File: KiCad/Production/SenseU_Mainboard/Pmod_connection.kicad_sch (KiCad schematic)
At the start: 1 part, among them J4 90122-0126

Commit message: assigning components
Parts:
- renumbered J4 to J3
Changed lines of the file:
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@@
         )
         (path "/43872b54-cf9c-4c7b-870d-631baccef0c0/915563dd-e56c-42ce-a954-58d654408565/fb835e06-d907-4f71-88e6-a872b0f9d18c"
-          (reference "#PWR064") (unit 1)
+          (reference "#PWR036") (unit 1)
         )
       )
@@
   (symbol (lib_id "SensU_Microphone_parts:90122-0126") (at 130.302 59.944 0) (unit 1)
     (in_bom yes) (on_board yes) (dnp no) (fields_autoplaced)
-    (property "Reference" "J4" (at 141.732 53.594 0)
+    (property "Reference" "J3" (at 141.732 53.594 0)
       (effects (font (size 1.27 1.27)))
     )
@@
       (project "SenseU_Mainboard"
         (path "/43872b54-cf9c-4c7b-870d-631baccef0c0/915563dd-e56c-42ce-a954-58d654408565/fb835e06-d907-4f71-88e6-a872b0f9d18c"
-          (reference "J4") (unit 1)
+          (reference "J3") (unit 1)
         )
       )
@@
         )
         (path "/43872b54-cf9c-4c7b-870d-631baccef0c0/915563dd-e56c-42ce-a954-58d654408565/fb835e06-d907-4f71-88e6-a872b0f9d18c"
-          (reference "#PWR065") (unit 1)
+          (reference "#PWR037") (unit 1)
         )
       )

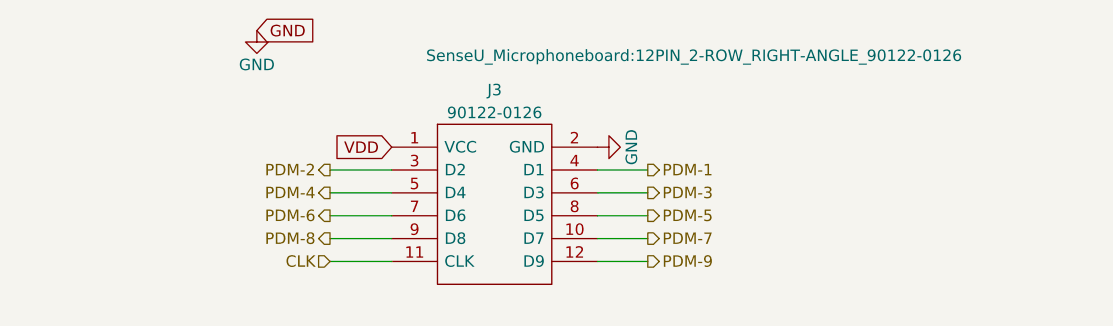
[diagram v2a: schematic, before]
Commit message: routing SenseU done
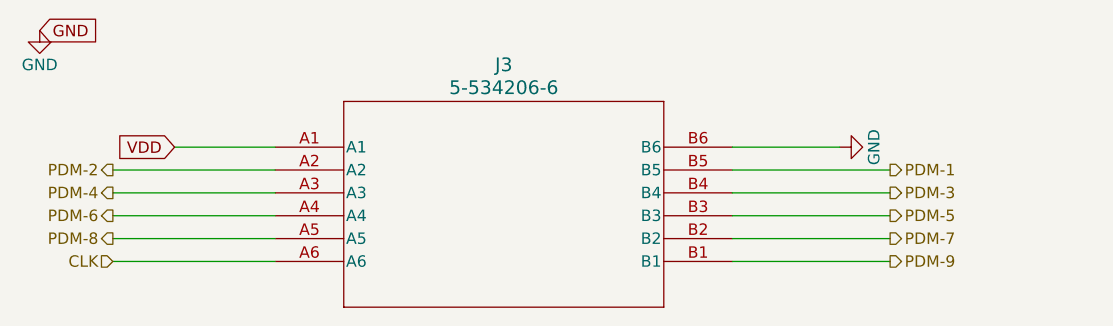
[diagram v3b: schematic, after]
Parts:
- removed J3: 90122-0126, SenseU_Microphoneboard:12PIN_2-ROW_RIGHT-ANGLE_90122-0126, symbol SensU_Microphone_parts:90122-0126
- added J3: 5-534206-6, PMOD:5-534206-6_TYC, symbol 2023-06-17_18-13-39:5-534206-6
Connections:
- net CLK: now also J3.A6
- net GND: now also J3.B6
- net PDM-1: now also J3.B5
- net PDM-2: now also J3.A2
- net PDM-3: now also J3.B4
- net PDM-4: now also J3.A3
- net PDM-5: now also J3.B3
- net PDM-6: now also J3.A4
- net PDM-7: now also J3.B2
- net PDM-8: now also J3.A5
- net PDM-9: now also J3.B1
- net VDD: now also J3.A1
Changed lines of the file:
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@@
 (kicad_sch (version 20230121) (generator eeschema)
   (paper "A4")
-  (wire (pts (xy 123.444 72.644) (xy 130.302 72.644))
+  (wire (pts (xy 99.314 72.644) (xy 117.348 72.644))
     (stroke (width 0) (type default))
   )
-  (wire (pts (xy 123.444 65.024) (xy 130.302 65.024))
+  (wire (pts (xy 99.314 65.024) (xy 117.348 65.024))
     (stroke (width 0) (type default))
   )
-  (wire (pts (xy 153.162 65.024) (xy 158.75 65.024))
+  (wire (pts (xy 106.172 59.944) (xy 117.348 59.944))
     (stroke (width 0) (type default))
   )
-  (wire (pts (xy 123.444 67.564) (xy 130.302 67.564))
+  (wire (pts (xy 168.148 65.024) (xy 185.674 65.024))
     (stroke (width 0) (type default))
   )
-  (wire (pts (xy 153.162 70.104) (xy 158.75 70.104))
+  (wire (pts (xy 99.314 67.564) (xy 117.348 67.564))
     (stroke (width 0) (type default))
   )
-  (wire (pts (xy 153.162 62.484) (xy 158.75 62.484))
+  (wire (pts (xy 168.148 70.104) (xy 185.674 70.104))
     (stroke (width 0) (type default))
   )
-  (wire (pts (xy 153.162 72.644) (xy 158.75 72.644))
+  (wire (pts (xy 168.148 62.484) (xy 185.674 62.484))
     (stroke (width 0) (type default))
   )
-  (wire (pts (xy 123.444 62.484) (xy 130.302 62.484))
+  (wire (pts (xy 99.314 62.484) (xy 117.348 62.484))
     (stroke (width 0) (type default))
   )
-  (wire (pts (xy 153.162 67.564) (xy 158.75 67.564))
+  (wire (pts (xy 168.148 67.564) (xy 185.674 67.564))
     (stroke (width 0) (type default))
   )
-  (wire (pts (xy 123.444 70.104) (xy 130.302 70.104))
+  (wire (pts (xy 168.148 72.644) (xy 185.674 72.644))
     (stroke (width 0) (type default))
   )
-  (global_label "VDD" (shape input) (at 130.302 59.944 180) (fields_autoplaced)
+  (wire (pts (xy 180.086 59.944) (xy 168.148 59.944))
+    (stroke (width 0) (type default))
+  )
+  (wire (pts (xy 99.314 70.104) (xy 117.348 70.104))
+    (stroke (width 0) (type default))
+  )
+  (global_label "VDD" (shape input) (at 106.172 59.944 180) (fields_autoplaced)
     (effects (font (size 1.27 1.27)) (justify right))
-    (property "Intersheetrefs" "${INTERSHEET_REFS}" (at 123.9435 59.944 0)
+    (property "Intersheetrefs" "${INTERSHEET_REFS}" (at 99.8135 59.944 0)
       (effects (font (size 1.27 1.27)) (justify right) hide)
     )
   )
-  (global_label "GND" (shape input) (at 115.316 46.99 0) (fields_autoplaced)
+  (global_label "GND" (shape input) (at 91.186 46.99 0) (fields_autoplaced)
     (effects (font (size 1.27 1.27)) (justify left))
-    (property "Intersheetrefs" "${INTERSHEET_REFS}" (at 121.8742 46.99 0)
+    (property "Intersheetrefs" "${INTERSHEET_REFS}" (at 97.7442 46.99 0)
       (effects (font (size 1.27 1.27)) (justify left) hide)
     )
   )
-  (hierarchical_label "PDM-7" (shape output) (at 158.75 70.104 0) (fields_autoplaced)
+  (hierarchical_label "PDM-7" (shape output) (at 185.674 70.104 0) (fields_autoplaced)
     (effects (font (size 1.27 1.27)) (justify left))
   )
-  (hierarchical_label "PDM-3" (shape output) (at 158.75 65.024 0) (fields_autoplaced)
+  (hierarchical_label "PDM-3" (shape output) (at 185.674 65.024 0) (fields_autoplaced)
     (effects (font (size 1.27 1.27)) (justify left))
   )
-  (hierarchical_label "PDM-8" (shape output) (at 123.444 70.104 180) (fields_autoplaced)
+  (hierarchical_label "PDM-8" (shape output) (at 99.314 70.104 180) (fields_autoplaced)
     (effects (font (size 1.27 1.27)) (justify right))
   )
-  (hierarchical_label "PDM-2" (shape output) (at 123.444 62.484 180) (fields_autoplaced)
+  (hierarchical_label "PDM-2" (shape output) (at 99.314 62.484 180) (fields_autoplaced)
     (effects (font (size 1.27 1.27)) (justify right))
   )
-  (hierarchical_label "PDM-5" (shape output) (at 158.75 67.564 0) (fields_autoplaced)
+  (hierarchical_label "PDM-5" (shape output) (at 185.674 67.564 0) (fields_autoplaced)
     (effects (font (size 1.27 1.27)) (justify left))
   )
-  (hierarchical_label "PDM-4" (shape output) (at 123.444 65.024 180) (fields_autoplaced)
+  (hierarchical_label "PDM-4" (shape output) (at 99.314 65.024 180) (fields_autoplaced)
     (effects (font (size 1.27 1.27)) (justify right))
   )
-  (hierarchical_label "CLK" (shape input) (at 123.444 72.644 180) (fields_autoplaced)
+  (hierarchical_label "CLK" (shape input) (at 99.314 72.644 180) (fields_autoplaced)
     (effects (font (size 1.27 1.27)) (justify right))
   )
-  (hierarchical_label "PDM-6" (shape output) (at 123.444 67.564 180) (fields_autoplaced)
+  (hierarchical_label "PDM-6" (shape output) (at 99.314 67.564 180) (fields_autoplaced)
     (effects (font (size 1.27 1.27)) (justify right))
   )
-  (hierarchical_label "PDM-9" (shape output) (at 158.75 72.644 0) (fields_autoplaced)
+  (hierarchical_label "PDM-9" (shape output) (at 185.674 72.644 0) (fields_autoplaced)
     (effects (font (size 1.27 1.27)) (justify left))
   )
-  (hierarchical_label "PDM-1" (shape output) (at 158.75 62.484 0) (fields_autoplaced)
+  (hierarchical_label "PDM-1" (shape output) (at 185.674 62.484 0) (fields_autoplaced)
     (effects (font (size 1.27 1.27)) (justify left))
   )
-  (symbol (lib_id "power:GND") (at 115.316 46.99 0) (unit 1)
+  (symbol (lib_id "power:GND") (at 91.186 46.99 0) (unit 1)
     (in_bom yes) (on_board yes) (dnp no)
-    (property "Reference" "#PWR024" (at 115.316 53.34 0)
+    (property "Reference" "#PWR024" (at 91.186 53.34 0)
       (effects (font (size 1.27 1.27)) hide)
     )
-    (property "Value" "GND" (at 115.316 50.8 0)
+    (property "Value" "GND" (at 91.186 50.8 0)
       (effects (font (size 1.27 1.27)))
     )
-    (property "Footprint" "" (at 115.316 46.99 0)
+    (property "Footprint" "" (at 91.186 46.99 0)
       (effects (font (size 1.27 1.27)) hide)
     )
-    (property "Datasheet" "" (at 115.316 46.99 0)
+    (property "Datasheet" "" (at 91.186 46.99 0)
       (effects (font (size 1.27 1.27)) hide)
     )
@@
     )
   )
-  (symbol (lib_id "SensU_Microphone_parts:90122-0126") (at 130.302 59.944 0) (unit 1)
+  (symbol (lib_id "2023-06-17_18-13-39:5-534206-6") (at 117.348 59.944 0) (unit 1)
     (in_bom yes) (on_board yes) (dnp no) (fields_autoplaced)
-    (property "Reference" "J3" (at 141.732 53.594 0)
-      (effects (font (size 1.27 1.27)))
+    (property "Reference" "J3" (at 142.748 50.8 0)
+      (effects (font (size 1.524 1.524)))
     )
-    (property "Value" "90122-0126" (at 141.732 56.134 0)
-      (effects (font (size 1.27 1.27)))
+    (property "Value" "5-534206-6" (at 142.748 53.34 0)
+      (effects (font (size 1.524 1.524)))
     )
-    (property "Footprint" "SenseU_Microphoneboard:12PIN_2-ROW_RIGHT-ANGLE_90122-0126" (at 134.112 49.784 0)
-      (effects (font (size 1.27 1.27)) (justify left))
+    (property "Footprint" "PMOD:5-534206-6_TYC" (at 117.348 59.944 0)
+      (effects (font (size 1.27 1.27) italic) hide)
     )
-    (property "Datasheet" "https://componentsearchengine.com/Datasheets/2/90122-0126.pdf" (at 108.712 42.164 0)
-      (effects (font (size 1.27 1.27)) (justify left) hide)
+    (property "Datasheet" "5-534206-6" (at 117.348 59.944 0)
+      (effects (font (size 1.27 1.27) italic) hide)
     )
-    (property "Description" "Headers & Wire Housings 2.54MM CGRIDIII HDR 12P R/A DR TIN" (at 111.252 44.704 0)
-      (effects (font (size 1.27 1.27)) (justify left) hide)
-    )
-    (property "Height" "6.15" (at 122.682 53.594 0)
-      (effects (font (size 1.27 1.27)) (justify left) hide)
-    )
-    (property "Mouser Part Number" "538-90122-0126" (at 112.522 48.514 0)
-      (effects (font (size 1.27 1.27)) (justify left) hide)
-    )
-    (property "Mouser Price/Stock" "https://www.mouser.co.uk/ProductDetail/Molex/90122-0126?qs=PvP5v7Eimsm0iCqn6boA0w%3D%3D" (at 106.172 38.354 0)
-      (effects (font (size 1.27 1.27)) (justify left) hide)
-    )
-    (property "Manufacturer_Name" "Molex" (at 139.192 73.914 0)
-      (effects (font (size 1.27 1.27)) (justify left) hide)
-    )
-    (property "Manufacturer_Part_Number" "90122-0126" (at 109.982 51.054 0)
-      (effects (font (size 1.27 1.27)) (justify left) hide)
-    )
-    (pin "1")
-    (pin "10")
-    (pin "11")
-    (pin "12")
-    (pin "2")
-    (pin "3")
-    (pin "4")
-    (pin "5")
-    (pin "6")
-    (pin "7")
-    (pin "8")
-    (pin "9")
+    (pin "A1")
+    (pin "A2")
+    (pin "A3")
+    (pin "A4")
+    (pin "A5")
+    (pin "A6")
+    (pin "B1")
+    (pin "B2")
+    (pin "B3")
+    (pin "B4")
+    (pin "B5")
+    (pin "B6")
     (instances
       (project "SenseU_Mainboard"
@@
         )
       )
-      (project "SenseU_Microphoneboard"
-        (path "/c15b751b-87a4-4d4e-aac0-7b5a75057e49"
-          (reference "J1") (unit 1)
-        )
-        (path "/c15b751b-87a4-4d4e-aac0-7b5a75057e49/08f64b92-ddeb-46a9-a410-79b61cc0149f"
-          (reference "J1") (unit 1)
-        )
-      )
     )
   )
-  (symbol (lib_id "power:GND") (at 153.162 59.944 90) (mirror x) (unit 1)
+  (symbol (lib_id "power:GND") (at 180.086 59.944 90) (mirror x) (unit 1)
     (in_bom yes) (on_board yes) (dnp no)
-    (property "Reference" "#PWR024" (at 159.512 59.944 0)
+    (property "Reference" "#PWR024" (at 186.436 59.944 0)
       (effects (font (size 1.27 1.27)) hide)
     )
-    (property "Value" "GND" (at 156.972 59.944 0)
+    (property "Value" "GND" (at 183.896 59.944 0)
       (effects (font (size 1.27 1.27)))
     )
-    (property "Footprint" "" (at 153.162 59.944 0)
+    (property "Footprint" "" (at 180.086 59.944 0)
       (effects (font (size 1.27 1.27)) hide)
     )
-    (property "Datasheet" "" (at 153.162 59.944 0)
+    (property "Datasheet" "" (at 180.086 59.944 0)
       (effects (font (size 1.27 1.27)) hide)
     )
